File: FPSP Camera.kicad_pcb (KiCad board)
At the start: 4 copper layers, 85.7 x 31.1 mm, 73 parts, among them J1 Conn_01x24_Socket, J2 Conn_01x02, J4 Conn_02x06_Top_Bottom, J5 Conn_02x06_Top_Bottom, SW1 PTS526_SM15_SMTR2_LFS, SW2 SW_Nidec_CAS-120A1, U1 LSM6DSL, U3 RP2350_60QFN, U4 TLV75533PDRV, U5 TLV73328PDRV, U6 TLV73315PDRV, Y1 SiT8008xx-1x-xxE

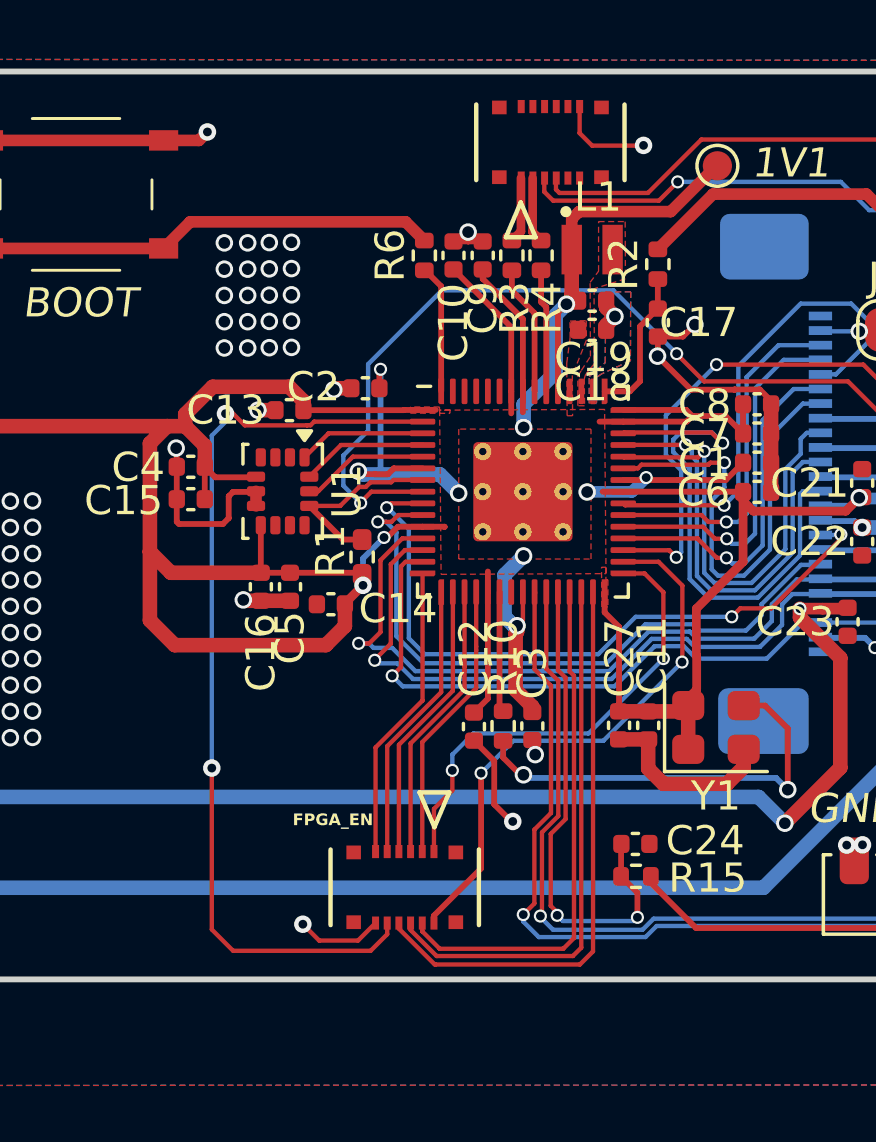
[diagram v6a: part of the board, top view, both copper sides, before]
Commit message: connector footprint swapped
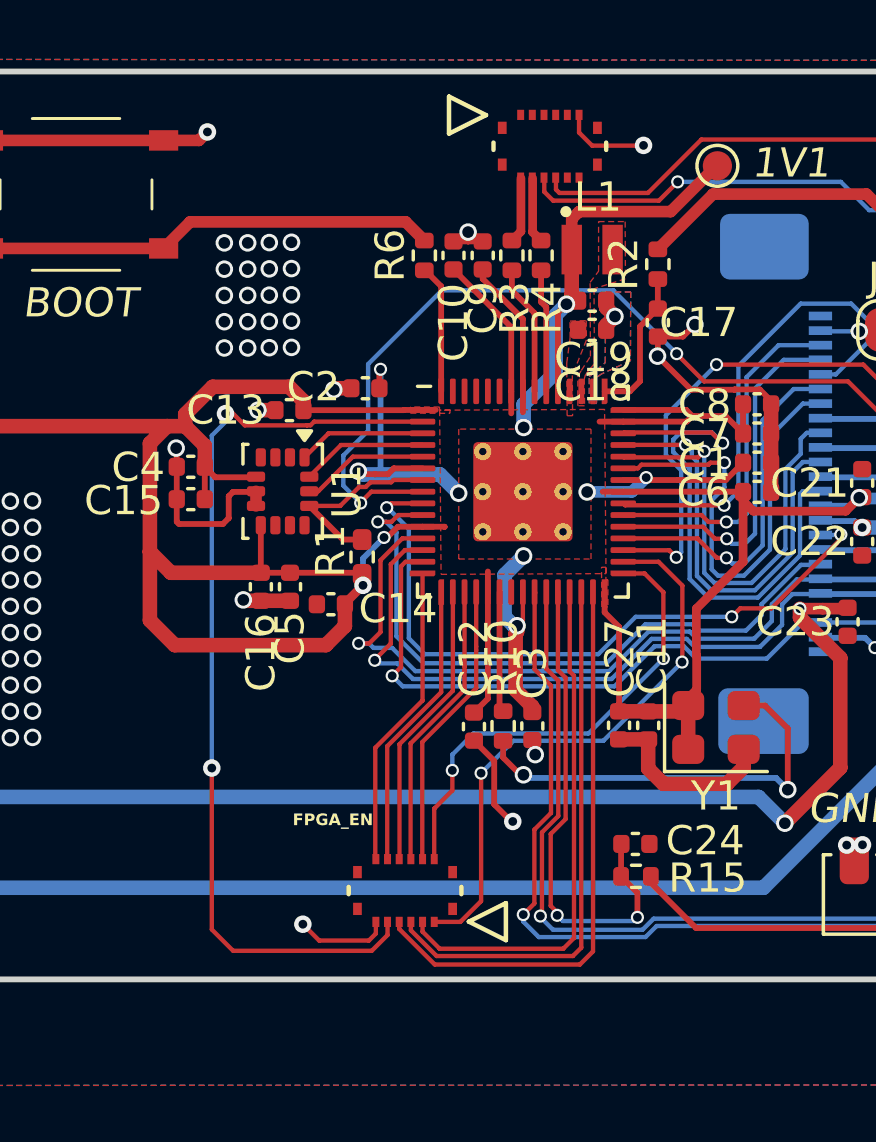
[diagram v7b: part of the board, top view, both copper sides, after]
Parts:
- J4, J5: footprint 5035481222:CON_5035481222 -> 5035521222:CON_5035521222
- moved J5 0.14 mm to (67.8, 18.5)
- moved J4 0.11 mm to (62.9, 44.0)
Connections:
- J4 pad 1: FPGA_CTRL -> HREF_OUT
- J4 pad 10: POSITION_OUT_CLK -> IMAGE_OUT_2
- J4 pad 11: POSITION_OUT_1 -> IMAGE_OUT_1
- J4 pad 12: AGND -> FPGA_EN
- J4 pad 2: IMAGE_OUT_4 -> IMAGE_CLK
- J4 pad 3: IMAGE_OUT_3 -> VSYNC_OUT
- J4 pad 4: IMAGE_OUT_2 -> POSITION_OUT_CLK
- J4 pad 5: IMAGE_OUT_1 -> POSITION_OUT_1
- J4 pad 6: FPGA_EN -> AGND
- J4 pad 7: HREF_OUT -> FPGA_CTRL
- J4 pad 8: IMAGE_CLK -> IMAGE_OUT_4
- J4 pad 9: VSYNC_OUT -> IMAGE_OUT_3
- J5 pad 1: /USB_D1+ -> unconnected-(J5-Pin_1-Pad1)
- J5 pad 10: unconnected-(J5-Pin_10-Pad10) -> /SWD_1
- J5 pad 12: AGND -> unconnected-(J5-Pin_12-Pad12)
- J5 pad 2: /USB_D1- -> unconnected-(J5-Pin_2-Pad2)
- J5 pad 3: /SWCLK_1 -> unconnected-(J5-Pin_3-Pad3)
- J5 pad 4: /SWD_1 -> unconnected-(J5-Pin_4-Pad4)
- J5 pad 6: unconnected-(J5-Pin_6-Pad6) -> AGND
- J5 pad 7: unconnected-(J5-Pin_7-Pad7) -> /USB_D1+
- J5 pad 8: unconnected-(J5-Pin_8-Pad8) -> /USB_D1-
- J5 pad 9: unconnected-(J5-Pin_9-Pad9) -> /SWCLK_1
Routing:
- net HREF_OUT: track 19.2 -> 19.7 mm

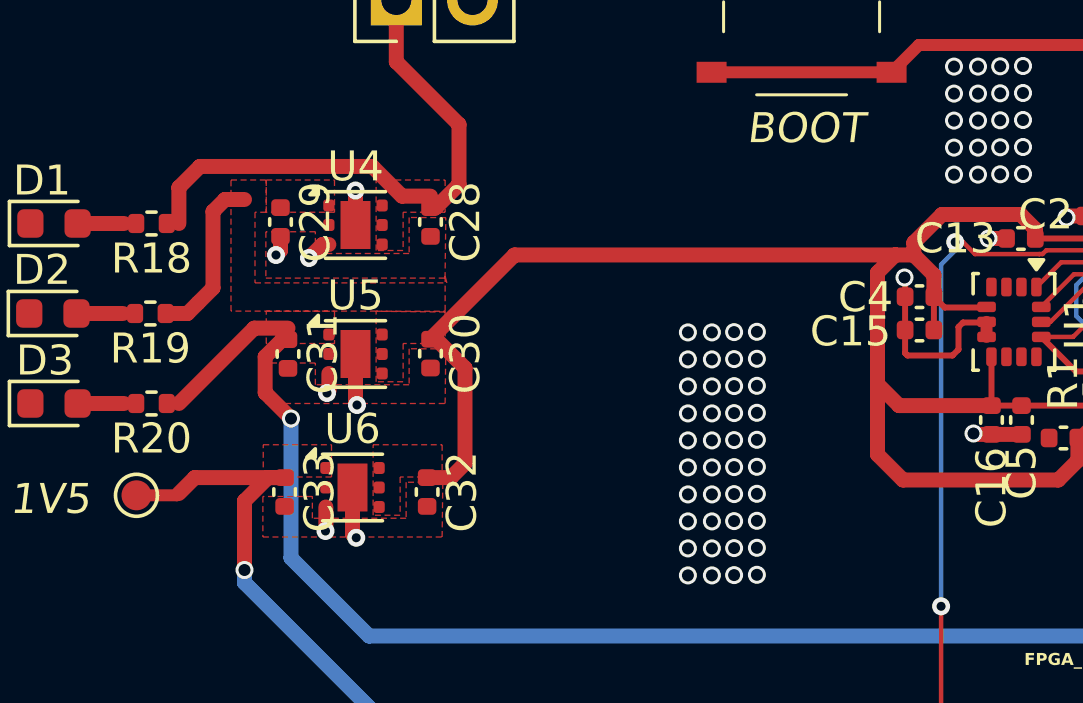
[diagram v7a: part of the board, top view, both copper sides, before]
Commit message: LDOs replaced
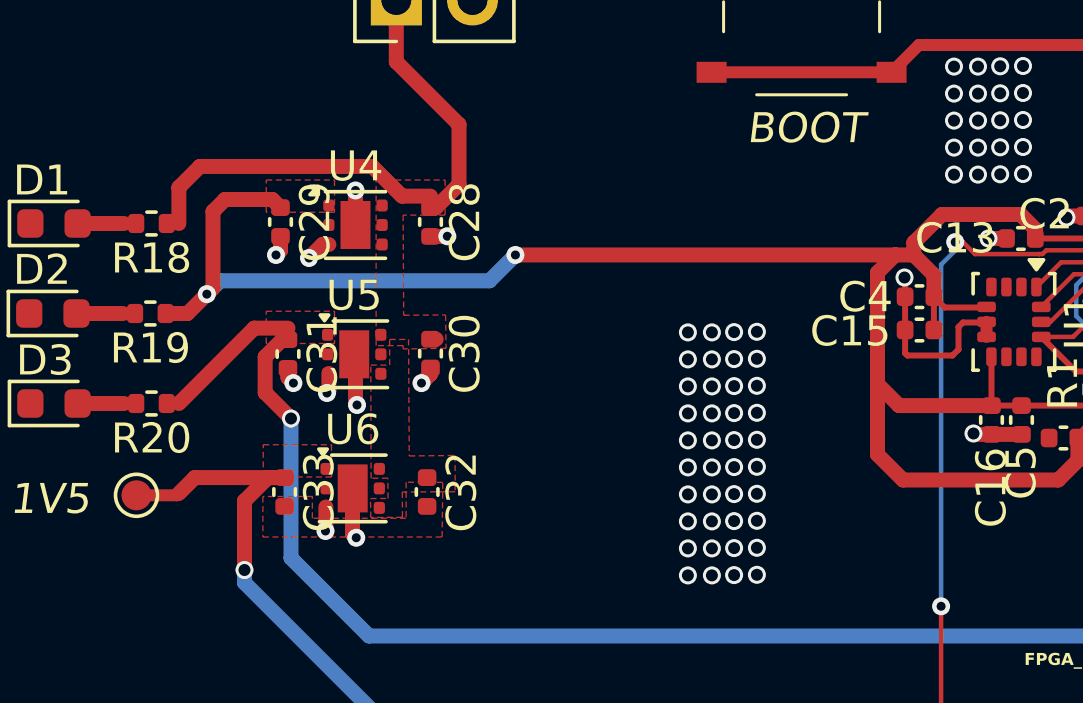
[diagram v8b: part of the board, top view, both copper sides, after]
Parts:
- U5: value TLV73328PDRV -> TLV75528PDRV
- U6: value TLV73315PDRV -> TLV75515PDRV
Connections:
- C30 pad 1: +3.3V -> +5V
- C32 pad 1: +3.3V -> +5V
- U5 pad 4: +3.3V -> +5V
- U5 pad 6: +3.3V -> +5V
- U6 pad 4: +3.3V -> +5V
- U6 pad 6: +3.3V -> +5V
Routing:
- net +3.3V: track 172.1 -> 174.1 mm, vias 4 -> 6
- net AGND: track 58.3 -> 60.1 mm, vias 125 -> 128
